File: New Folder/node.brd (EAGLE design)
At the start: 30 x 40 mm, 11 parts, among them IC1 TINY24/44/84-SSU

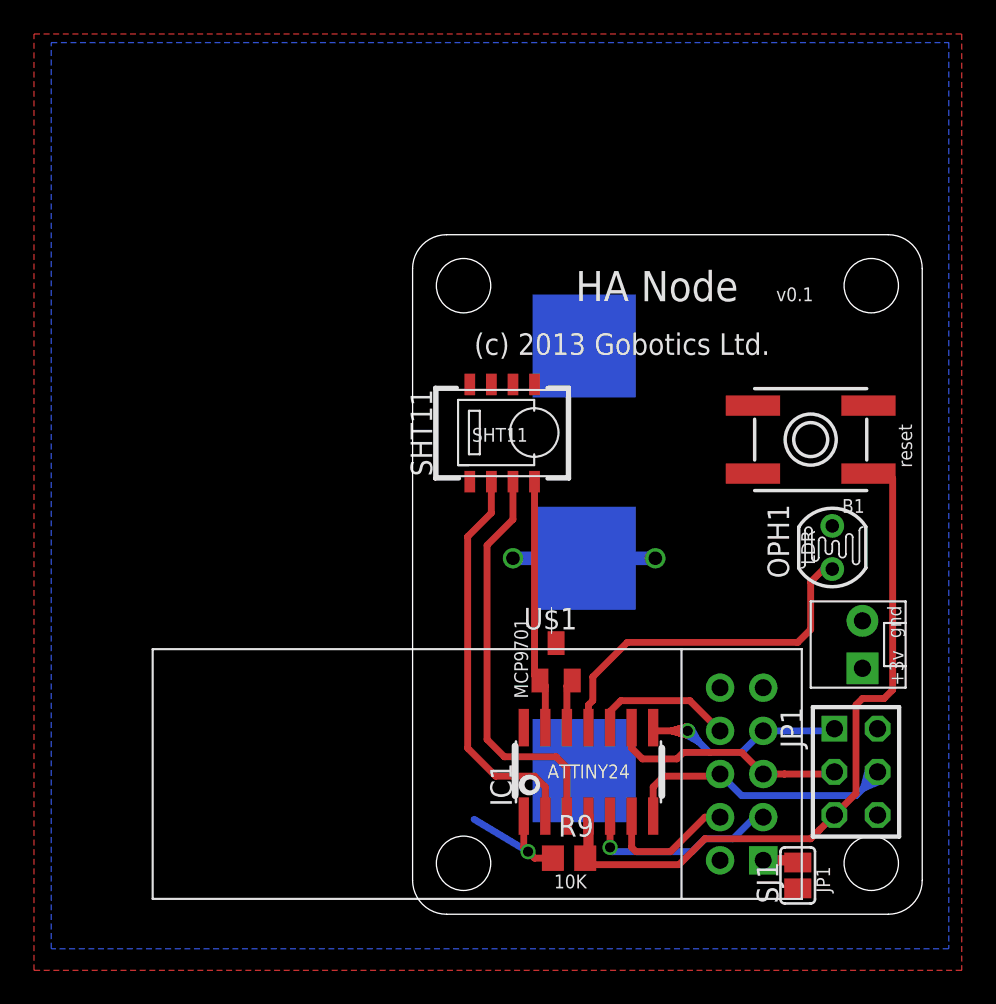
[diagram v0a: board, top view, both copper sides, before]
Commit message: Added HA node v0.2, now with battery voltage monitoring
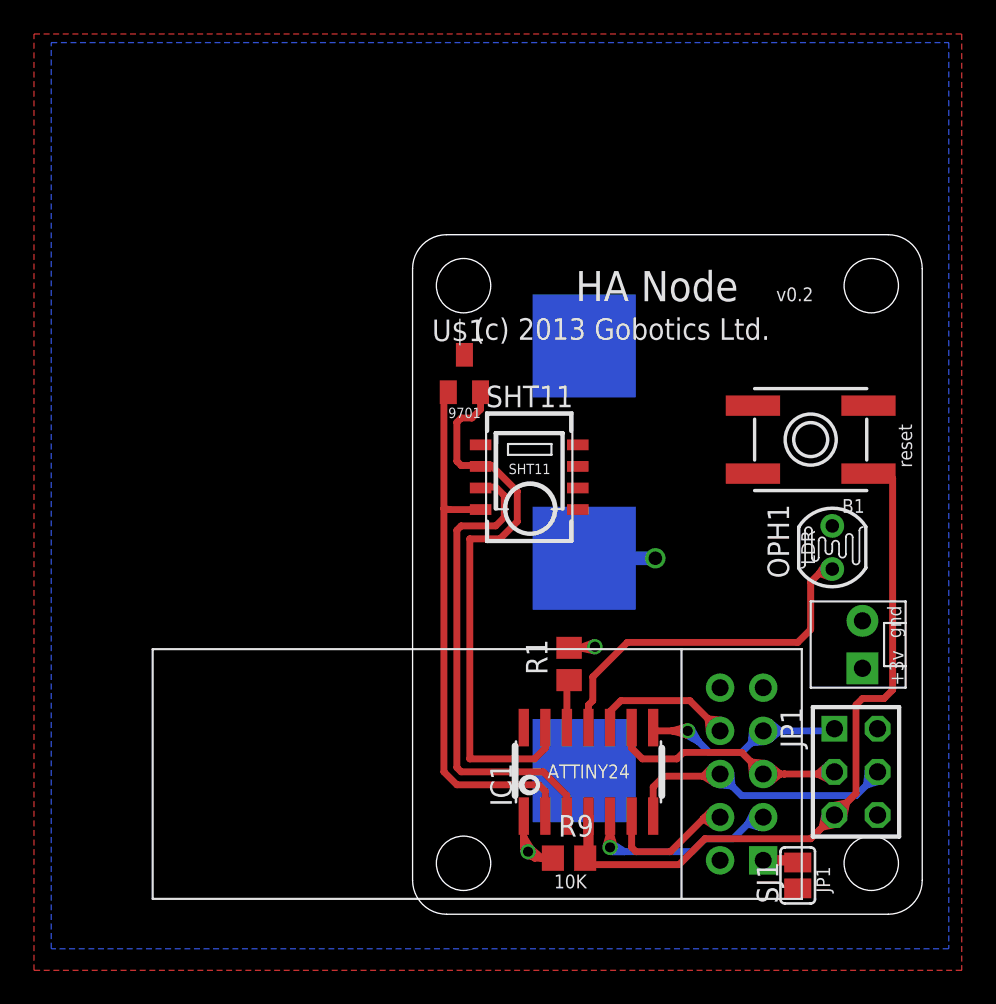
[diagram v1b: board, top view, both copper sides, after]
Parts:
- added R1: 47k, rcl:R0805
- moved U$1 17.8 mm to (23.1, 31.8)
- moved SHT1 7.75 mm to (22.4, 21.3), turned to 0 degrees
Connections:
- removed net DATA: IC1.2, SHT1.DATA
- removed net SPARE: IC1.12, U$1.2
- new net TEMP: IC1.13, SHT1.DATA, U$1.2
- new net VBATT: IC1.12, R1.1
- net VCC: now also R1.2
- net VDD: now also IC1.2; no longer IC1.13
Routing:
- net TEMP: track 0.00 -> 33.2 mm
- net DATA: track 23.5 -> 0.00 mm
- net VDD: track 14.7 -> 32.5 mm
- net SCK: track 14.1 -> 22.6 mm
- net CE: track 12.2 -> 19.5 mm
- net RESET: track 42.2 -> 47.8 mm
- net MOSI: track 19.8 -> 24.9 mm
- net VCC: track 7.52 -> 12.0 mm, vias 1 -> 2
- net GND: track 8.51 -> 4.19 mm, vias 2 -> 1
- net CLK: track 24.1 -> 28.3 mm
- net SPARE: track 2.90 -> 0.00 mm
- net VBATT: track 0.00 -> 2.85 mm
- net CSN: track 8.00 -> 10.8 mm
- net IRQ: track 8.43 -> 11.2 mm
- net LDR: track 21.5 -> 23.7 mm
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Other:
- board text added: "9701"
- board text added: "v0.2"
- board text removed: "MCP9701"
- board text removed: "v0.1"
